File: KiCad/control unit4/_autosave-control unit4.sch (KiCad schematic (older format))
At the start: 40 parts, among them J1 Conn_01x02_Female, J2 Conn_01x03_Female, J3 Conn_01x03_Female, J4 Conn_01x02_Female, J5 Conn_01x02_Female, U1 LM358, U2 LM358

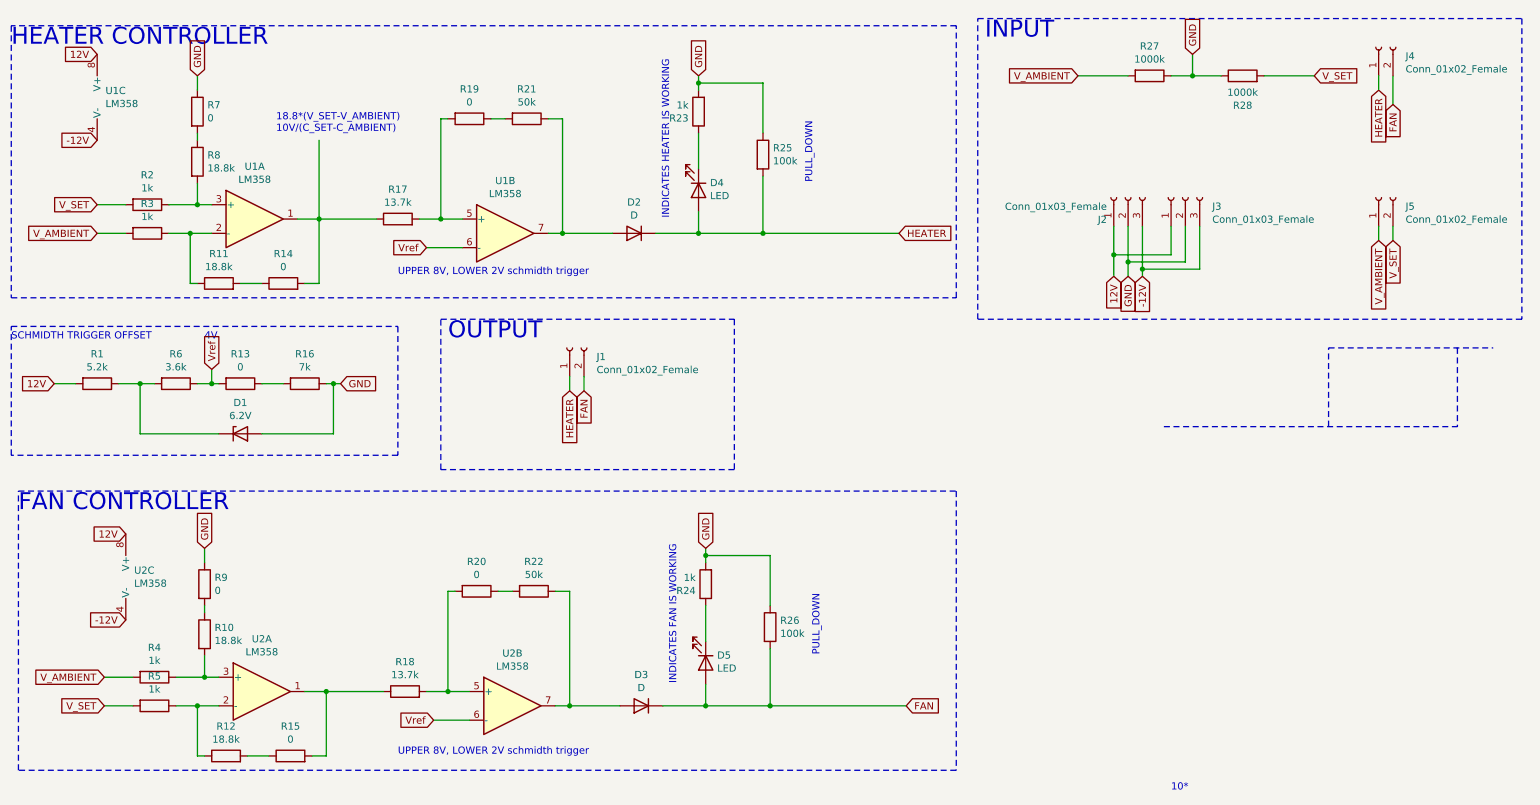
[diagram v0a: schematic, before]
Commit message: PCB of Control unit 4 is finished
.
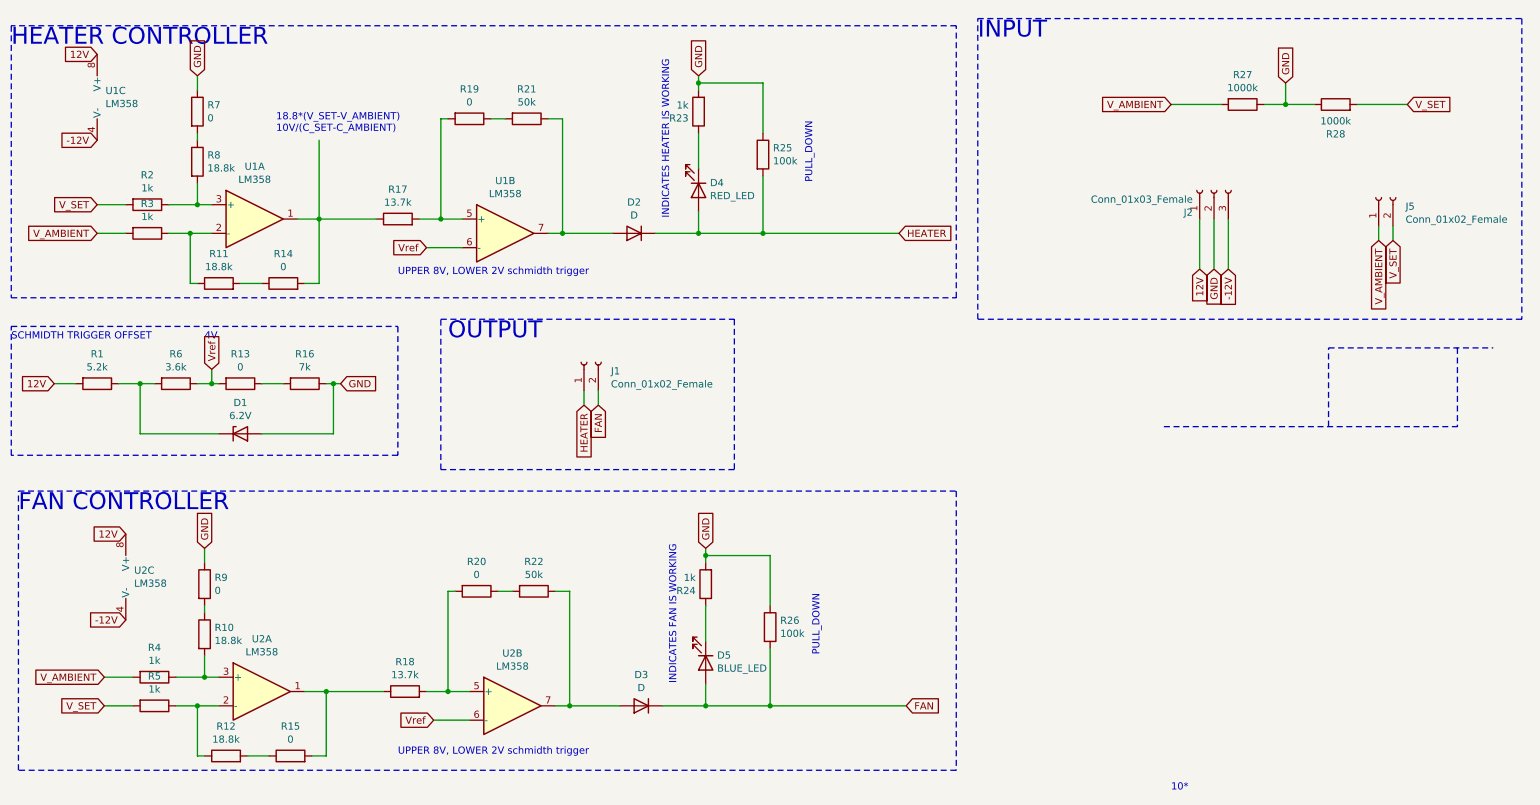
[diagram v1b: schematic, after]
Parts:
- removed J3: Conn_01x03_Female, symbol Connector:Conn_01x03_Female
- removed J4: Conn_01x02_Female, symbol Connector:Conn_01x02_Female
- D1, D2, D3: footprint (none) -> Diode_THT:D_5W_P12.70mm_Horizontal
- D4: value LED -> RED_LED; footprint (none) -> LED_THT:LED_D3.0mm_FlatTop
- D5: value LED -> BLUE_LED; footprint (none) -> LED_THT:LED_D3.0mm_FlatTop
- J1, J5: footprint (none) -> TerminalBlock:TerminalBlock_Altech_AK300-2_P5.00mm
- J2: footprint (none) -> TerminalBlock:TerminalBlock_Altech_AK300-3_P5.00mm
- R1, R10, R11, R12, R13, R14, R15, R16, R17, R18, R19, R2, R20, R21, R22, R23, R24, R25, R26, R27, R28, R3, R4, R5, R6, R7, R8, R9: footprint (none) -> Resistor_THT:R_Axial_DIN0309_L9.0mm_D3.2mm_P12.70mm_Horizontal
- U1, U2: footprint (none) -> Package_DIP:DIP-8_W7.62mm
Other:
- moved on the sheet: J1, J2, R27, R28
